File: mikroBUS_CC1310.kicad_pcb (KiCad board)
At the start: 2 copper layers, 25.4 x 28.6 mm, 4 parts, among them P1 Val**, P2 Val**

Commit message: Some progress in layout.
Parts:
- added C1: 12pF, Capacitors_SMD:C_0402, F.Cu at (117.3, 115.3)
- added C10: 100pF, Capacitors_SMD:C_0402, F.Cu at (116.1, 110.6)
- added C11: 3.6pF, Capacitors_SMD:C_0402, F.Cu at (117.1, 110.6)
- added C12: 100nF, Capacitors_SMD:C_0402, F.Cu at (121.7, 110.7)
- added C13: 100nF, Capacitors_SMD:C_0402, F.Cu at (126.5, 121.4)
- added C14: 2.7pF, Capacitors_SMD:C_0402, F.Cu at (118.5, 109.3)
- added C15: DNP, Capacitors_SMD:C_0402, F.Cu at (141.2, 115.7)
- added C16: DNP, Capacitors_SMD:C_0402, F.Cu at (120.4, 110.7)
- added C17: 100nF, Capacitors_SMD:C_0402, F.Cu at (125.0, 110.7)
- added C18: 22uF, Capacitors_SMD:C_0603, F.Cu at (130.3, 113.5)
- added C19: 6.2pF, Capacitors_SMD:C_0402, F.Cu at (118.5, 107.8)
- added C2: 1uF, Capacitors_SMD:C_0402, F.Cu at (141.2, 113.9)
- added C20: DNP, Capacitors_SMD:C_0402, F.Cu at (141.2, 112.1)
- added C21: 100nF, Capacitors_SMD:C_0402, F.Cu at (130.6, 114.8)
- added C22: 3pF, Capacitors_SMD:C_0402, F.Cu at (118.5, 106.8)
- added C23: DNP, Capacitors_SMD:C_0603, F.Cu at (130.3, 112.0)
- added C24: 100pF, Capacitors_SMD:C_0402, F.Cu at (117.1, 105.5)
- added C3: 100nF, Capacitors_SMD:C_0402, F.Cu at (142.6, 107.8)
- added C4: 22uF, Capacitors_SMD:C_0603, F.Cu at (130.8, 118.2)
- added C5: DNP, Capacitors_SMD:C_0603, F.Cu at (116.8, 122.6)
- added C6: 12pF, Capacitors_SMD:C_0402, F.Cu at (117.3, 117.6)
- added C7: 3.6pF, Capacitors_SMD:C_0402, F.Cu at (119.0, 110.7)
- added C8: 100nF, Capacitors_SMD:C_0402, F.Cu at (123.7, 110.7)
- added C9: 100nF, Capacitors_SMD:C_0402, F.Cu at (121.9, 121.4)
- added FL1: BLM18HE152SN1, Passive:0603, F.Cu at (116.8, 120.0)
- added J1: u.FL, Connector:U.FL-R-SMT, F.Cu at (117.3, 100.7)
- added J2: SMA, Connector:SMA_EDGE, F.Cu at (123.7, 97.9)
- added L1: 27nH, Passive:0402, F.Cu at (118.5, 112.3)
- added L2: 6.8uH, Passive:0805, F.Cu at (130.6, 116.6)
- added L4: 7.5nH, Passive:0402, F.Cu at (116.8, 112.3)
- added L5: 7.5nH, Passive:0402, F.Cu at (118.0, 110.7)
- added L6: 6.8nH, Passive:0402, F.Cu at (117.1, 108.8)
- added L7: 6.8nH, Passive:0402, F.Cu at (117.1, 107.3)
- added P3: JTAG, Header:HEADER_M_2.54MM_2R8P_ST_AU_PTH, F.Cu at (142.7, 121.3)
- added R1: 100k, Passive:0402, F.Cu at (140.2, 107.8)
- added Y1: 32.768kHz, Passive:FC_135, F.Cu at (119.1, 116.3)
- added Y2: 24MHz, Passive:SX_3225, F.Cu at (122.7, 108.0)
- P1, P2: value Val** -> HEADER_M_2.54MM_1R8P_ST_AU_PTH
- U1: renamed from VQFN48; value VAL** -> CC1310F128RGZ
- moved ? 2.39 mm to (124.7, 116.6)
- moved U1 1.73 mm to (124.7, 116.1)
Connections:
- P1 pad 1: (no net) -> AN
- P1 pad 2: (no net) -> nRESET
- P1 pad 3: (no net) -> CS
- P1 pad 4: (no net) -> SCK
- P1 pad 5: (no net) -> MISO
- P1 pad 6: (no net) -> MOSI
- P1 pad 7: (no net) -> +3.3V
- P1 pad 8: (no net) -> GND
- P2 pad 1: (no net) -> PWM
- P2 pad 2: (no net) -> INT
- P2 pad 3: (no net) -> RX
- P2 pad 4: (no net) -> TX
- P2 pad 5: (no net) -> SCL
- P2 pad 6: (no net) -> SDA
- P2 pad 7: (no net) -> +5V
- P2 pad 8: (no net) -> GND
- U1 pad 1: (no net) -> RF_P
- U1 pad 10: (no net) -> MOSI
- U1 pad 11: (no net) -> PWM
- U1 pad 12: (no net) -> INT
- U1 pad 13: (no net) -> VDD
- U1 pad 14: (no net) -> RX
- U1 pad 15: (no net) -> TX
- U1 pad 16: (no net) -> SCL
- U1 pad 17: (no net) -> SDA
- U1 pad 18: (no net) -> Net-(U1-Pad18)
- U1 pad 19: (no net) -> Net-(U1-Pad19)
- U1 pad 2: (no net) -> RF_N
- U1 pad 20: (no net) -> Net-(U1-Pad20)
- U1 pad 21: (no net) -> Net-(U1-Pad21)
- U1 pad 22: (no net) -> VDD
- U1 pad 23: (no net) -> Net-(C2-Pad1)
- U1 pad 24: (no net) -> JTAG_TMS
- U1 pad 25: (no net) -> JTAG_TCK
- U1 pad 26: (no net) -> JTAG_TDO
- U1 pad 27: (no net) -> JTAG_TDI
- U1 pad 28: (no net) -> Net-(U1-Pad28)
- U1 pad 29: (no net) -> Net-(U1-Pad29)
- U1 pad 3: (no net) -> RF_RXTX
- U1 pad 30: (no net) -> Net-(U1-Pad30)
- U1 pad 31: (no net) -> Net-(U1-Pad31)
- U1 pad 32: (no net) -> Net-(U1-Pad32)
- U1 pad 33: (no net) -> DCDC_SW
- U1 pad 34: (no net) -> VDD
- U1 pad 35: (no net) -> nRESET
- U1 pad 36: (no net) -> Net-(U1-Pad36)
- U1 pad 37: (no net) -> Net-(U1-Pad37)
- U1 pad 38: (no net) -> Net-(U1-Pad38)
- U1 pad 39: (no net) -> Net-(U1-Pad39)
- U1 pad 4: (no net) -> X32K_Q1
- U1 pad 40: (no net) -> Net-(U1-Pad40)
- U1 pad 41: (no net) -> Net-(U1-Pad41)
- U1 pad 42: (no net) -> Net-(U1-Pad42)
- U1 pad 43: (no net) -> Net-(U1-Pad43)
- U1 pad 44: (no net) -> VDD
- U1 pad 45: (no net) -> VEE
- U1 pad 46: (no net) -> X24M_N
- U1 pad 47: (no net) -> X24M_P
- U1 pad 48: (no net) -> VEE
- U1 pad 49: (no net) -> GND
- U1 pad 5: (no net) -> X32K_Q2
- U1 pad 6: (no net) -> AN
- U1 pad 7: (no net) -> CS
- U1 pad 8: (no net) -> SCK
- U1 pad 9: (no net) -> MISO
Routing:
- net GND: track 0.00 -> 17.5 mm, vias 0 -> 14
- net ANT: track 0.00 -> 12.3 mm
- net RF_N: track 0.00 -> 6.18 mm
- net X32K_Q2: track 0.00 -> 5.50 mm
- net RF_P: track 0.00 -> 4.79 mm
- net VDD: track 0.00 -> 4.54 mm, vias 0 -> 1
- net X24M_P: track 0.00 -> 4.22 mm
- net X24M_N: track 0.00 -> 4.19 mm
- net X32K_Q1: track 0.00 -> 4.13 mm
- net VEE: track 0.00 -> 4.11 mm
- net DCDC_SW: track 0.00 -> 2.70 mm
- net Net-(C11-Pad1): track 0.00 -> 2.63 mm
- net Net-(C22-Pad1): track 0.00 -> 1.65 mm
- net Net-(C19-Pad1): track 0.00 -> 1.50 mm
- net RF_RXTX: track 0.00 -> 1.23 mm
- added copper zone on Pwr.Cu, net +3.3V
- added copper zone on Gnd.Cu, net GND
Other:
- copper layers 2 -> 4
- net class Default: clearance 0.2 -> 0.1524; trace_width 0.25 -> 0.1524; via_dia 0.6 -> 0.4572; via_drill 0.4 -> 0.254
- net class GPIO added: clearance 0.1524, trace_width 0.1524, via_dia 0.4572, via_drill 0.254
- net class Ground added: clearance 0.1524, trace_width 0.3048, via_dia 0.4572, via_drill 0.254
- net class Power added: clearance 0.1524, trace_width 0.3048, via_dia 0.4572, via_drill 0.254
- net class RF_Feed added: clearance 0.1524, trace_width 0.254, via_dia 0.4572, via_drill 0.254
- net class RF_Pi added: clearance 0.1524, trace_width 0.1524, via_dia 0.4572, via_drill 0.254
- rule trace_clearance: 0.2 -> 0.1524
- rule trace_min: 0.2 -> 0.127
- rule via_min_drill: 0.3 -> 0.254
- rule via_min_size: 0.4 -> 0.4572
- board text added: "CC1310 mikroBUS"
- board text added: "HW REV. 0.01"
- board text removed: "Board Name"
- board text removed: "HW REV. X.XX"

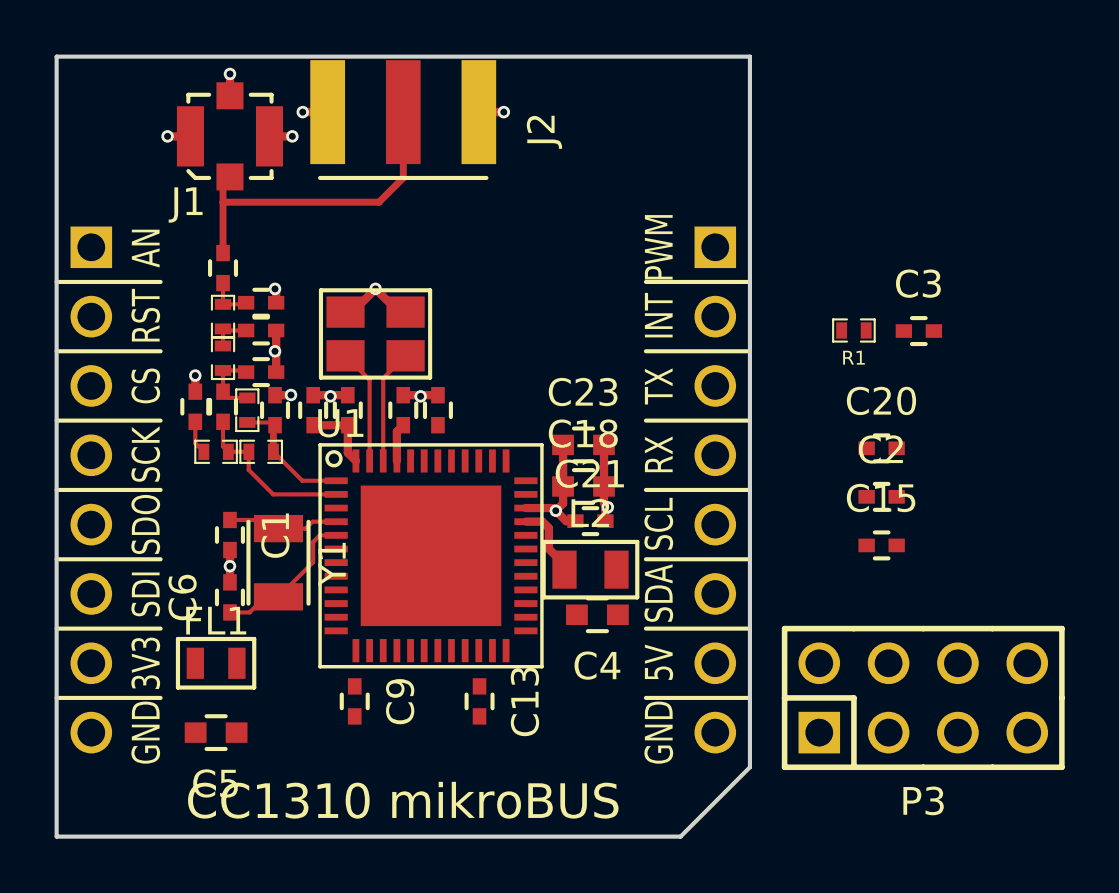
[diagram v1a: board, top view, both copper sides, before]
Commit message: Layout for RF impedance match network completed.  Added spring antenna and through-hole SMA straight connector as options.
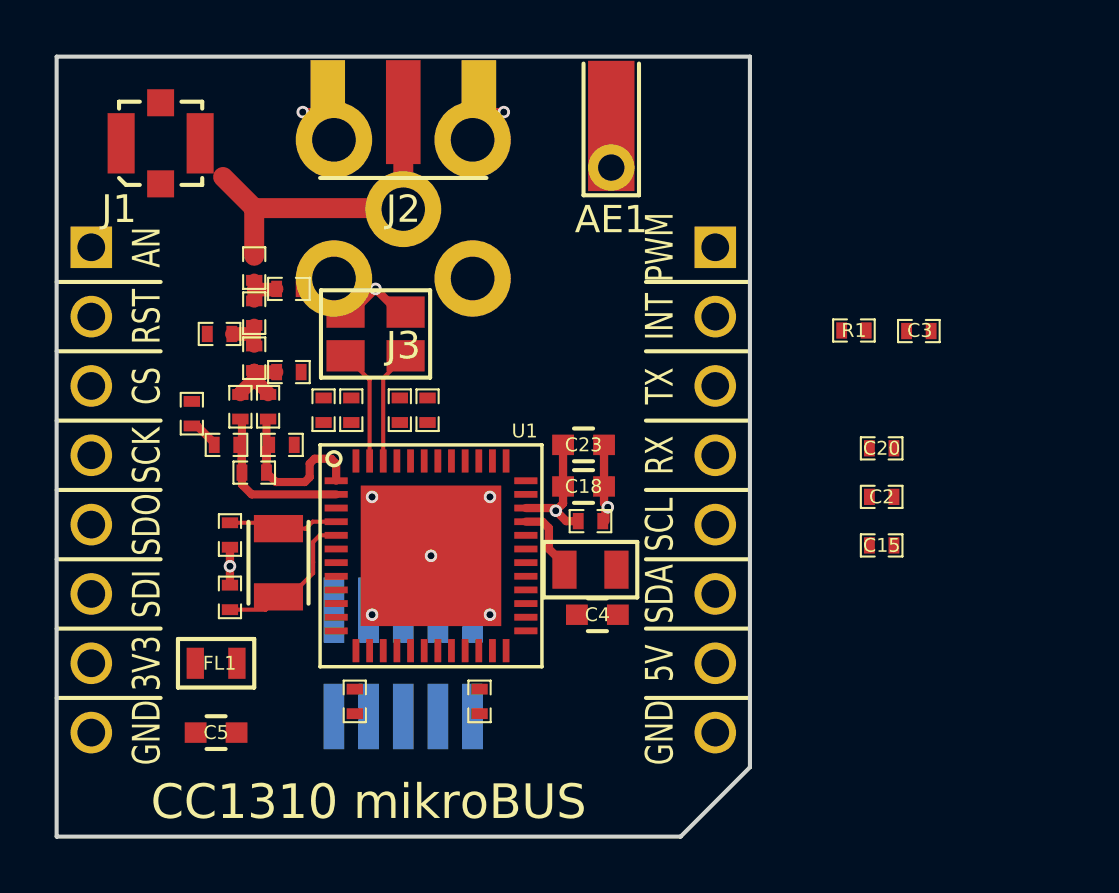
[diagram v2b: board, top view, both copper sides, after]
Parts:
- added AE1: 915MHz Spring, Passive:ANTENNA_HELICAL_RA, F.Cu at (131.3, 101.9)
- added J3: SMA Straight, Connector:SMA_STRAIGHT_SOCKET, F.Cu at (123.7, 103.4)
- C1, C10, C11, C12, C13, C14, C15, C16, C17, C19, C2, C20, C21, C22, C24, C3, C6, C7, C8, C9: footprint Capacitors_SMD:C_0402 -> Passive:0402
- P3: footprint Header:HEADER_M_2.54MM_2R8P_ST_AU_PTH -> Header:HEADER_50MIL_2R10P_SMT; moved to B.Cu
- moved P3 19.1 mm to (123.7, 120.0)
- moved ? 4.31 mm to (123.7, 112.4)
- moved J1 2.55 mm to (114.8, 101.0)
- moved C19 1.53 mm to (117.0, 108.0), turned to 180 degrees
- moved C7 1.30 mm to (119.3, 112.0), turned to 0 degrees
- moved L7 1.15 mm to (118.2, 107.2)
- moved C24 1.14 mm to (118.2, 105.5)
- moved L6 1.14 mm to (118.2, 108.8)
- moved C22 1.14 mm to (119.5, 106.3)
- moved C14 1.02 mm to (119.5, 109.3)
- moved L1 0.80 mm to (118.2, 113.0)
- moved L5 0.77 mm to (118.7, 110.6)
- moved C11 0.64 mm to (117.7, 110.6)
- moved L4 0.46 mm to (117.2, 112.0)
- moved C16 0.38 mm to (120.8, 110.7)
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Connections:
- net Net-(C11-Pad1) renamed /RF_Match1
- net Net-(C19-Pad1) renamed /RF_Match2
- net Net-(C22-Pad1) renamed /RF_Match3
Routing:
- net VEE: track 4.11 -> 0.00 mm
- net GND: track 17.5 -> 15.3 mm, vias 14 -> 9
- net RF_P: track 4.79 -> 6.59 mm
- net ANT: track 12.3 -> 11.7 mm
- net nRESET: vias 0 -> 1
- added copper zone on B.Cu, net GND
- added copper zone on F.Cu, net VDD
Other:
- net class RF_Bal added: clearance 0.1524, trace_width 0.299999, via_dia 0.4572, via_drill 0.254
- net class RF_Feed: trace_width 0.254 -> 0.729996
- net class RF_Pi: trace_width 0.1524 -> 0.499999
- board text added: "Check 0402 footprints for silkscreen/soldermask overlap"
- board text added: "Check SMA Edge footprint to ensure top and bottom pads are not soldermasked"
- board text added: "Need to compare network to TI's reference design layout"
